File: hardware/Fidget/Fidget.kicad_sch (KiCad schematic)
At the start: 10 parts

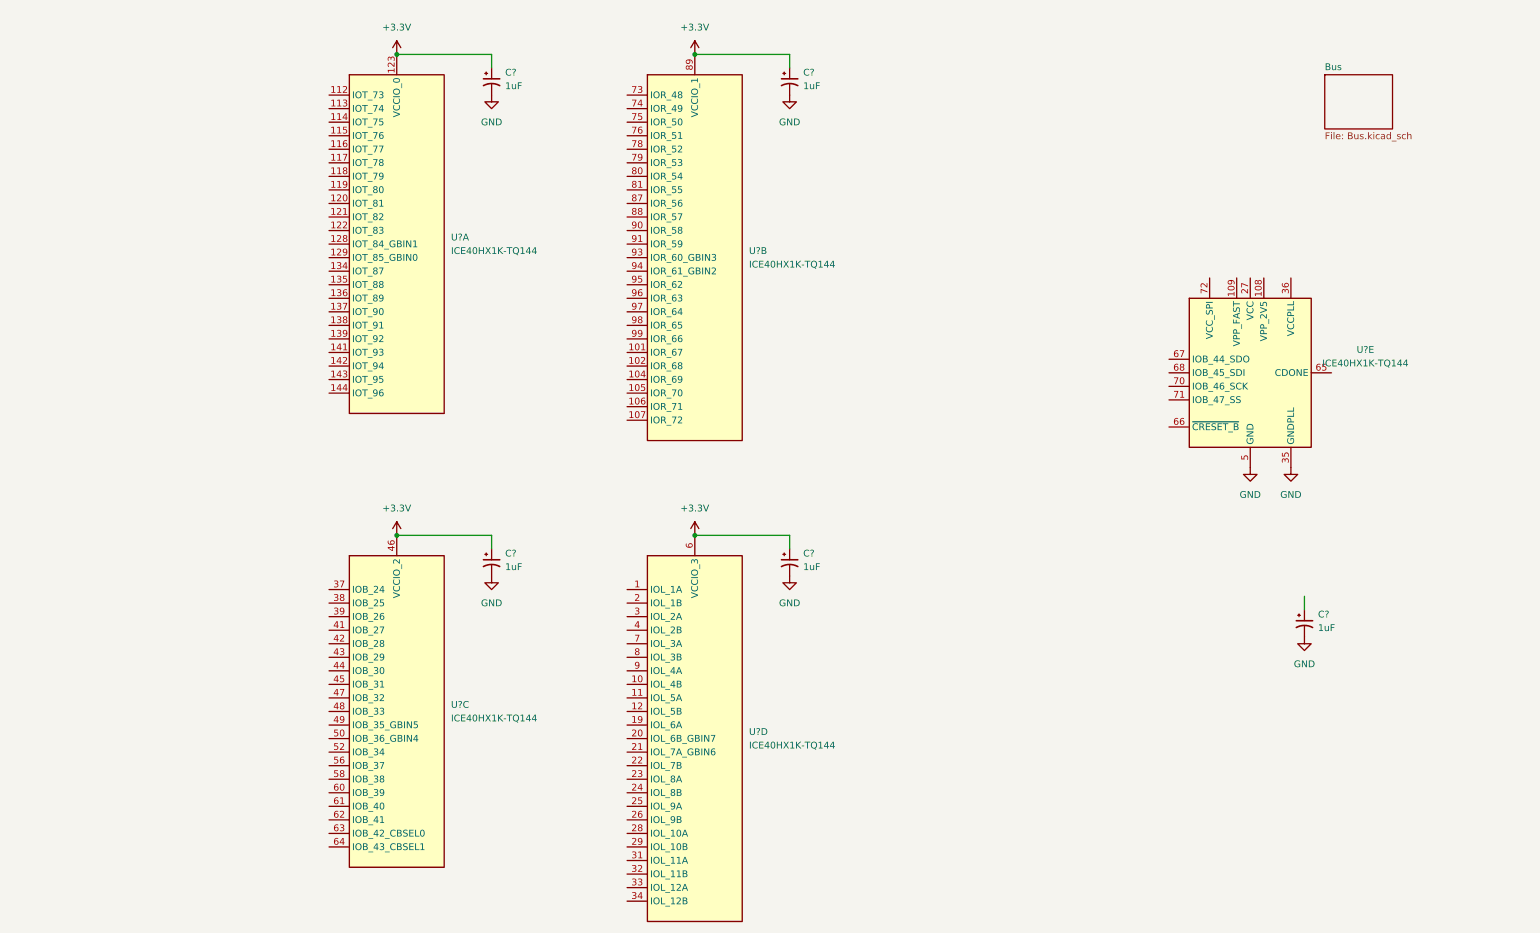
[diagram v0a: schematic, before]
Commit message: Added level shifting and some I/O assignments
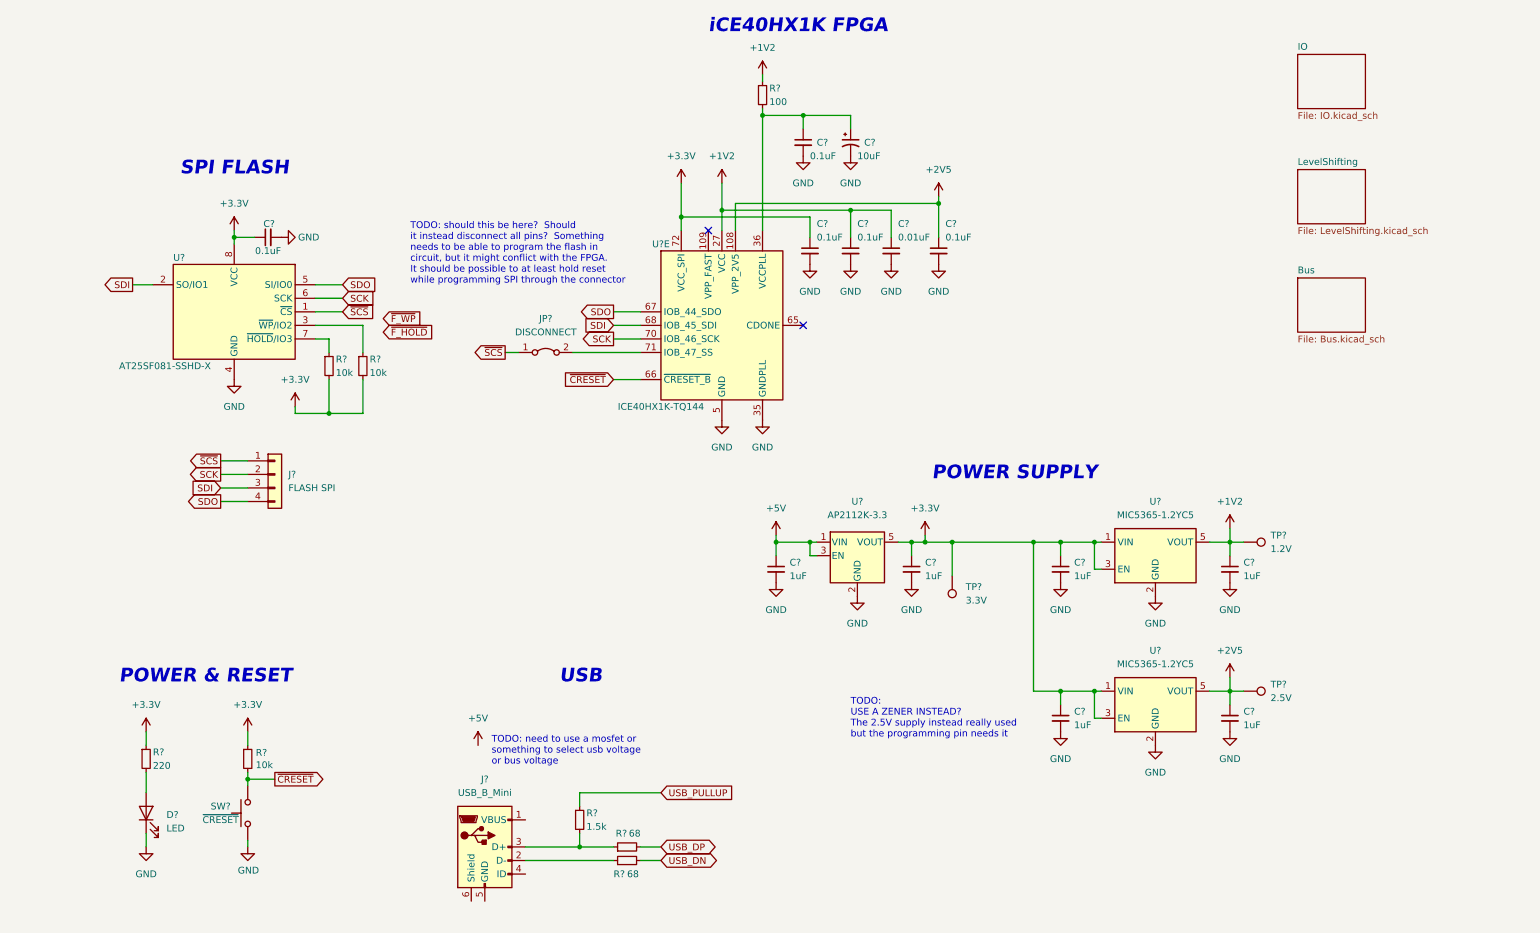
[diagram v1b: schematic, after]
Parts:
- removed C? (x5): 1uF, symbol Device:C_Polarized_Small_US
- removed U? (x4): ICE40HX1K-TQ144, Package_QFP:TQFP-144_20x20mm_P0.5mm, symbol FPGA_Lattice:ICE40HX1K-TQ144
- added C?: 0.01uF, symbol Device:C_Small
- added C?: 10uF, symbol Device:C_Polarized_Small_US
- added C? (x5): 0.1uF, symbol Device:C_Small
- added C? (x6): 1uF, symbol Device:C_Small
- added D?: LED, symbol Device:LED
- added J?: FLASH SPI, symbol Connector_Generic:Conn_01x04
- added J?: USB_B_Mini, symbol Connector:USB_B_Mini
- added JP?: DISCONNECT, symbol Jumper:Jumper_2_Bridged
- added R? (x2): 68, symbol Device:R_Small
- added R?: 10k, Resistor_THT:R_Axial_DIN0204_L3.6mm_D1.6mm_P5.08mm_Horizontal, symbol Device:R_Small
- added R? (x2): 10k, symbol Device:R_Small
- added R?: 220, symbol Device:R_Small
- added R?: 1.5k, symbol Device:R_Small
- added R?: 100, symbol Device:R_Small
- added SW?: ~{CRESET}, Button_Switch_THT:SW_PUSH_6mm, symbol Switch:SW_Push
- added TP?: 3.3V, symbol Connector:TestPoint
- added TP?: 2.5V, symbol Connector:TestPoint
- added TP?: 1.2V, symbol Connector:TestPoint
- added U? (x2): MIC5365-1.2YC5, Package_TO_SOT_SMD:SOT-353_SC-70-5, symbol Regulator_Linear:MIC5365-3.3YC5
- added U?: AP2112K-3.3, Package_TO_SOT_SMD:SOT-23-5, symbol Regulator_Linear:AP2112K-3.3
- added U?: AT25SF081-SSHD-X, Package_SO:SOIC-8_3.9x4.9mm_P1.27mm, symbol Memory_Flash:AT25SF081-SSHD-X
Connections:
- net +3.3V: now also U?.72 (VCC_SPI), C?.1, C?.1, C?.1, C?.1, C?.1, R?.1, R?.1, R?.2, R?.2, TP?.1, U?.1 (VIN), U?.1 (VIN), U?.3 (EN), U?.3 (EN), U?.5 (VOUT), U?.8 (VCC)
- net GND: now also C?.2, C?.2, C?.2, C?.2, C?.2, C?.2, C?.2, C?.2, C?.2, C?.2, C?.2, C?.2, C?.2, D?.1 (K), SW?.1, U?.2 (GND), U?.2 (GND), U?.2 (GND), U?.4 (GND)
- net +2V5: now reaches U?.108 (VPP_2V5)
- net +2V5: now also C?.1, C?.1, TP?.1, U?.5 (VOUT)
- net +1V2: now reaches U?.111 (VCC), U?.27 (VCC), U?.51 (VCC), U?.92 (VCC)
- net +1V2: now also C?.1, C?.1, C?.1, R?.1, TP?.1, U?.5 (VOUT)
- net at U?.36 (VCCPLL): now also C?.1, C?.1, R?.2
- net ~{CRESET}: now reaches U?.66 (~{CRESET_B})
- net ~{CRESET}: now also R?.2, SW?.2
- net SDO: now reaches U?.67 (IOB_44_SDO)
- net SDO: now also J?.4 (Pin_4), U?.5 (SI/IO0)
- net SDI: now reaches U?.68 (IOB_45_SDI)
- net SDI: now also J?.3 (Pin_3), U?.2 (SO/IO1)
- net SCK: now reaches U?.70 (IOB_46_SCK)
- net SCK: now also J?.2 (Pin_2), U?.6 (SCK)
- net at U?.71 (IOB_47_SS): now also JP?.2 (B)
- new net: J?.2 (D-), R?.1
- new net: R?.1, U?.3 (~{WP}/IO2)
- new net: D?.2 (A), R?.2
- new net: J?.3 (D+), R?.1, R?.2
- new net: R?.1, U?.7 (~{HOLD}/IO3)
- new net +5V: C?.1, U?.1 (VIN), U?.3 (EN)
- new net USB_DN: R?.2
- new net USB_DP: R?.2
- new net USB_PULLUP: R?.1
- new net ~{SCS}: J?.1 (Pin_1), JP?.1 (A), U?.1 (~{CS})
- no-connect marks 0 -> 2
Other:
- added sheet IO (IO.kicad_sch)
- added sheet LevelShifting (LevelShifting.kicad_sch)
- note added: "POWER & RESET"
- note added: "POWER SUPPLY"
- note added: "SPI FLASH"
- note added: "TODO: USE A ZENER INSTEAD? The 2.5V supply instead really used but the programming pin needs it"
- note added: "TODO: need to use a mosfet or something to select usb voltage or bus voltage"
- note added: "TODO: should this be here? Should it instead disconnect all pins? Something needs to be able to program the flash in circuit, but it might conflict with the FPGA. It should be possible to at least hold reset while programming SPI through the connector"
- note added: "USB"
- note added: "iCE40HX1K FPGA"
- moved on the sheet: U?E

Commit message: Added oscillators
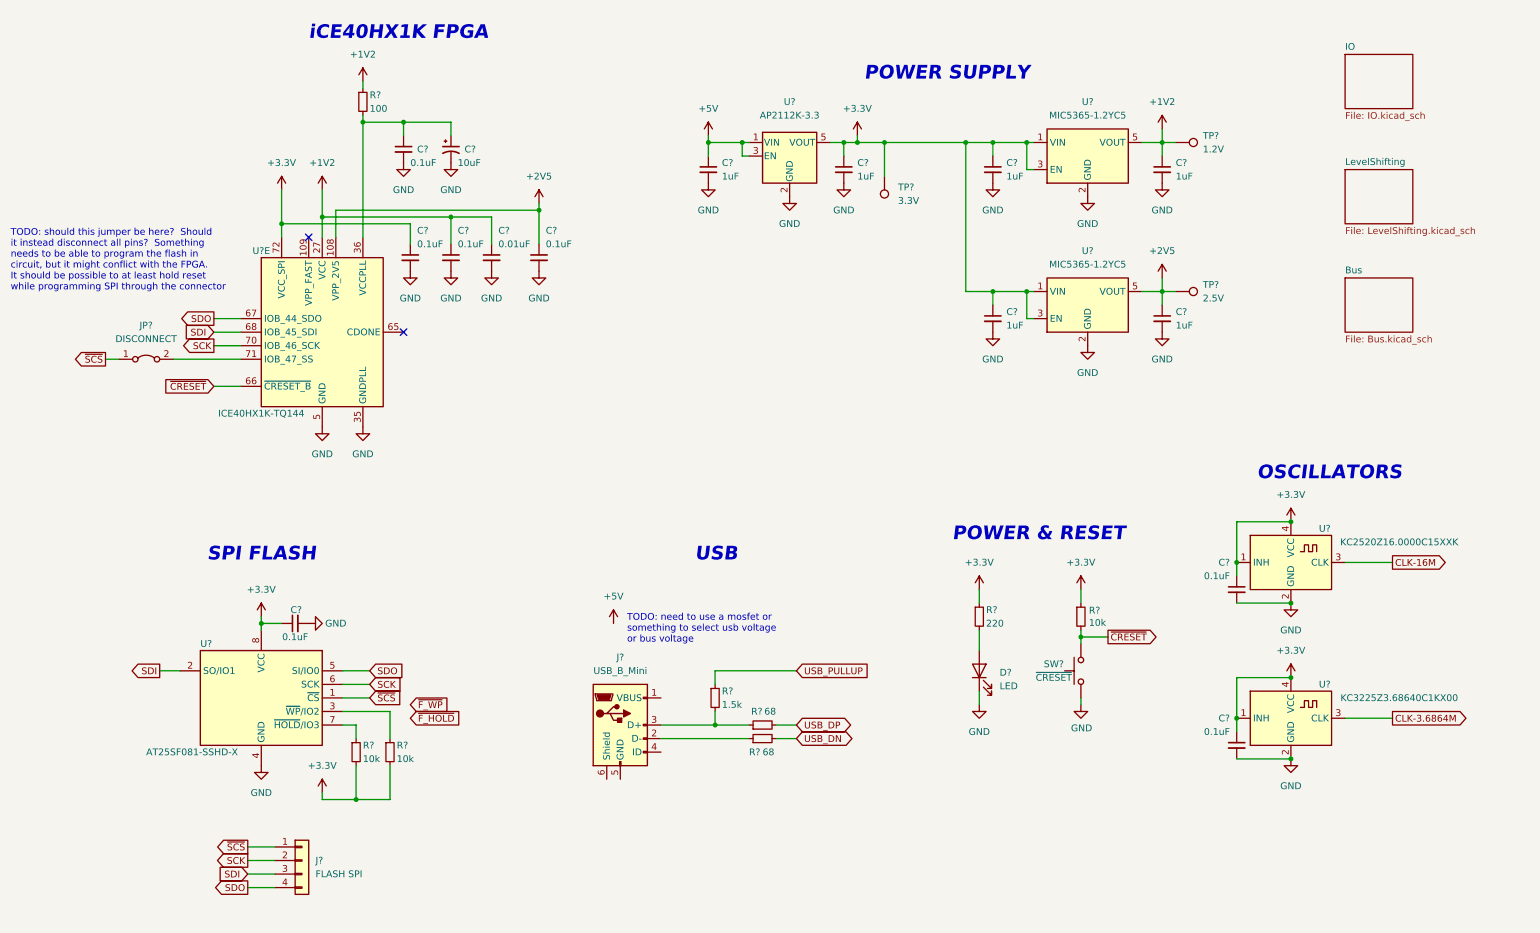
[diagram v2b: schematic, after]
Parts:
- added C? (x2): 0.1uF, symbol Device:C_Small
- added U?: KC2520Z16.0000C15XXK, Oscillator:Oscillator_SMD_Kyocera_KC2520Z-4Pin_2.5x2.0mm, symbol Oscillator:KC2520Z
- added U?: KC3225Z3.68640C1KX00, Oscillator:Oscillator_SMD_Kyocera_KC2520Z-4Pin_2.5x2.0mm, symbol Oscillator:KC2520Z
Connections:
- net +3.3V: now also C?.1, C?.1, U?.1 (INH), U?.1 (INH), U?.4 (VCC), U?.4 (VCC)
- net GND: now also C?.2, C?.2, U?.2 (GND), U?.2 (GND)
- new net CLK-16M: U?.3 (CLK)
- new net CLK-3.6864M: U?.3 (CLK)
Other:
- note added: "OSCILLATORS"
- note added: "TODO: should this jumper be here? Should it instead disconnect all pins? Something needs to be able to program the flash in circuit, but it might conflict with the FPGA. It should be possible to at least hold reset while programming SPI through the connector"
- note removed: "TODO: USE A ZENER INSTEAD? The 2.5V supply instead really used but the programming pin needs it"
- note removed: "TODO: should this be here? Should it instead disconnect all pins? Something needs to be able to program the flash in circuit, but it might conflict with the FPGA. It should be possible to at least hold reset while programming SPI through the connector"
- moved on the sheet: C?, D?, J?, JP?, R?, SW?, TP?, U?, U?E

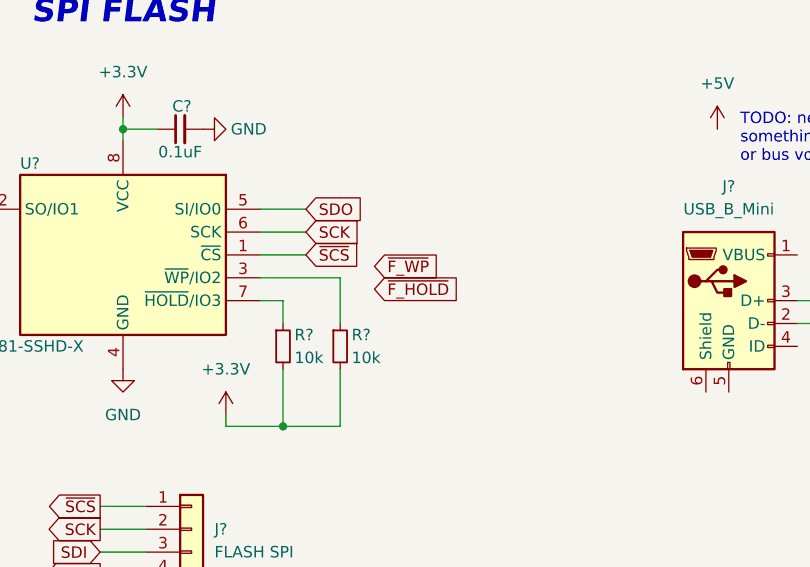
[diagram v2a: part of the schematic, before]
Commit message: Assigned bus control signals to level shifters
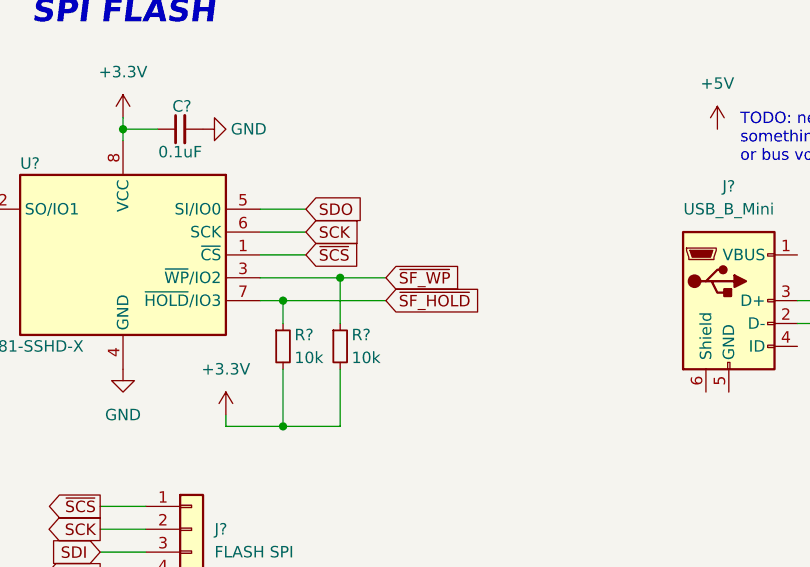
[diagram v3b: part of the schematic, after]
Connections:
- net ~{SF_WP}: now reaches R?.1, U?.3 (~{WP}/IO2)
- net ~{SF_HOLD}: now reaches R?.1, U?.7 (~{HOLD}/IO3)
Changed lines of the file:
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@@
   (junction (at 52.07 129.54) (diameter 0) (color 0 0 0 0)
   )
+  (junction (at 76.2 146.05) (diameter 0) (color 0 0 0 0)
+  )
   (junction (at 195.58 39.37) (diameter 0) (color 0 0 0 0)
   )
@@
   )
   (junction (at 135.89 39.37) (diameter 0) (color 0 0 0 0)
+  )
+  (junction (at 69.85 148.59) (diameter 0) (color 0 0 0 0)
   )
   (junction (at 163.83 39.37) (diameter 0) (color 0 0 0 0)
@@
     (stroke (width 0) (type default) (color 0 0 0 0))
   )
+  (wire (pts (xy 76.2 146.05) (xy 81.28 146.05))
+    (stroke (width 0) (type default) (color 0 0 0 0))
+  )
   (wire (pts (xy 63.5 53.34) (xy 87.63 53.34))
     (stroke (width 0) (type default) (color 0 0 0 0))
@@
   )
   (wire (pts (xy 205.74 143.51) (xy 205.74 144.78))
+    (stroke (width 0) (type default) (color 0 0 0 0))
+  )
+  (wire (pts (xy 69.85 148.59) (xy 81.28 148.59))
     (stroke (width 0) (type default) (color 0 0 0 0))
   )
@@
     )
   )
-  (global_label "~{F_HOLD}" (shape input) (at 80.01 147.32 0) (fields_autoplaced)
-    (effects (font (size 1.27 1.27)) (justify left))
-    (property "Intersheet References" "${INTERSHEET_REFS}" (id 0) (at 89.4383 147.2406 0)
+  (global_label "~{SF_HOLD}" (shape input) (at 81.28 148.59 0) (fields_autoplaced)
+    (effects (font (size 1.27 1.27)) (justify left))
+    (property "Intersheet References" "${INTERSHEET_REFS}" (id 0) (at 91.9179 148.5106 0)
       (effects (font (size 1.27 1.27)) (justify left) hide)
     )
@@
     )
   )
-  (global_label "~{F_WP}" (shape input) (at 80.01 144.78 0) (fields_autoplaced)
-    (effects (font (size 1.27 1.27)) (justify left))
-    (property "Intersheet References" "${INTERSHEET_REFS}" (id 0) (at 87.2007 144.7006 0)
-      (effects (font (size 1.27 1.27)) (justify left) hide)
-    )
+  (global_label "~{SF_WP}" (shape input) (at 81.28 146.05 0) (fields_autoplaced)
+    (effects (font (size 1.27 1.27)) (justify left))
+    (property "Intersheet References" "${INTERSHEET_REFS}" (id 0) (at 89.6802 145.9706 0)
+      (effects (font (size 1.27 1.27)) (justify left) hide)
+    )
